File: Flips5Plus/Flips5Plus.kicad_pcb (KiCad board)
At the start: 2 copper layers, 80 x 75 mm, 8 parts, among them CN1 Conn_02x30_Odd_Even, CN2 UFP2810, CN3 UFP2810, U1 FP2800A, U2 FP2800A

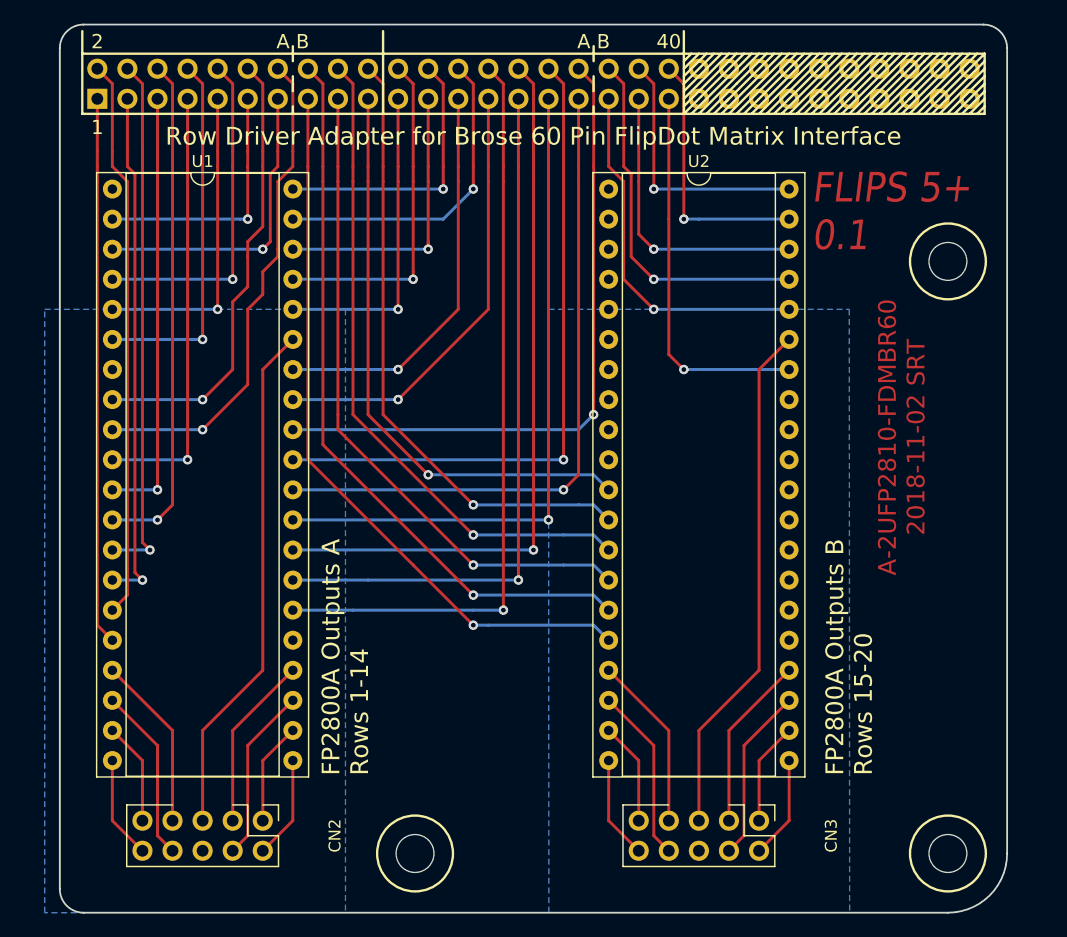
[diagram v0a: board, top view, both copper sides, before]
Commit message: using ANGLED shrouded header
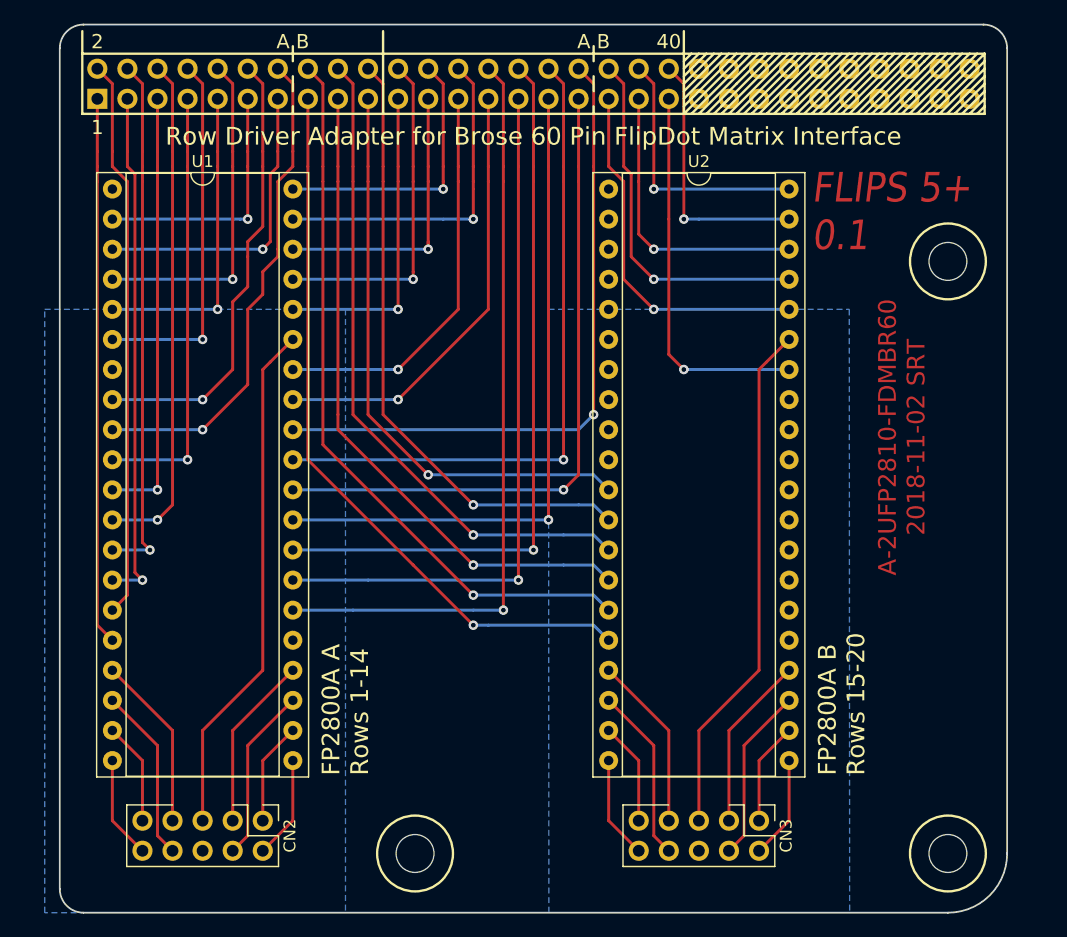
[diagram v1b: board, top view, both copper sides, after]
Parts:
- CN2, CN3: footprint Own:Pin_Header_Straight_Shrouded_2x05_Pitch2.54mm -> Own:Pin_Header_Angle_Shrouded_2x05_Pitch2.54mm
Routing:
- net Net-(CN1-Pad26): track 27.0 -> 28.5 mm
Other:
- board text added: "FP2800A A Rows 1-14"
- board text added: "FP2800A B Rows 15-20"
- board text removed: "FP2800A Outputs A Rows 1-14"
- board text removed: "FP2800A Outputs B Rows 15-20"

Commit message: adding logos and 3d models
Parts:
- added REF**: KiCAD Logo, Symbols:Symbol_KiCAD-Logo_CopperAndSilkScreenTop, F.Cu at (143.5, 115.6)
- added REF***: OSHW-Logo2_7.3x6mm_SilkScreen, Symbols:OSHW-Logo2_7.3x6mm_SilkScreen, F.Cu at (143.5, 130.2)
- added REF***: WEEE-Logo_4.2x6mm_SilkScreen, Symbols:WEEE-Logo_4.2x6mm_SilkScreen, B.Cu at (105.4, 147.3)
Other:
- board text added: "FLIPS"
- board text added: "FP2800A A: Rows 1-14"
- board text added: "FP2800A B: Rows 15-20"
- board text added: "SRT Flips 5Plus V1.0 2018-11-02 github.com/cawapy/FlipSuite"
- board text added: "back"
- board text added: "front"
- board text removed: "A-2UFP2810-FDMBR60 2018-11-02 SRT"
- board text removed: "FLIPS 5+ 0.1"
- board text removed: "FP2800A A Rows 1-14"
- board text removed: "FP2800A B Rows 15-20"

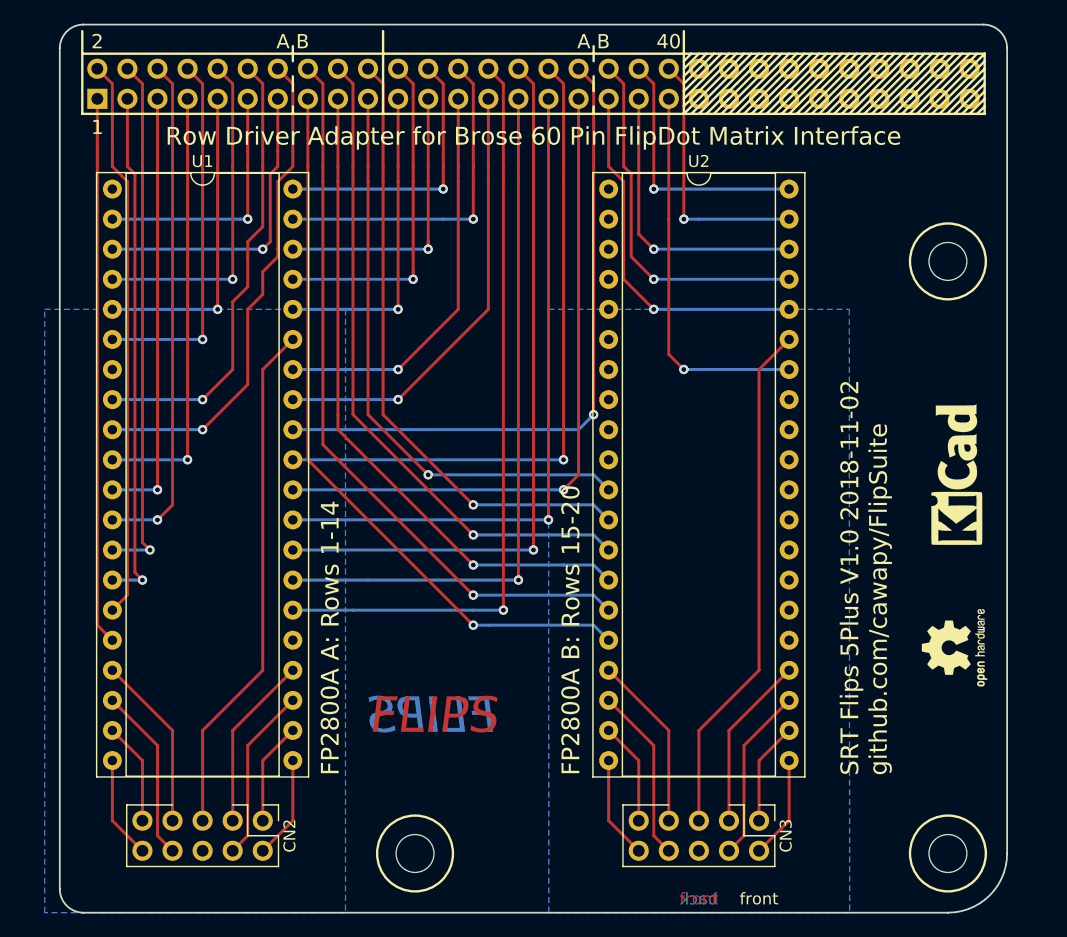
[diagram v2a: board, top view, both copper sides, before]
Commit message: rearranging mounting holes and symbols fixing measurements
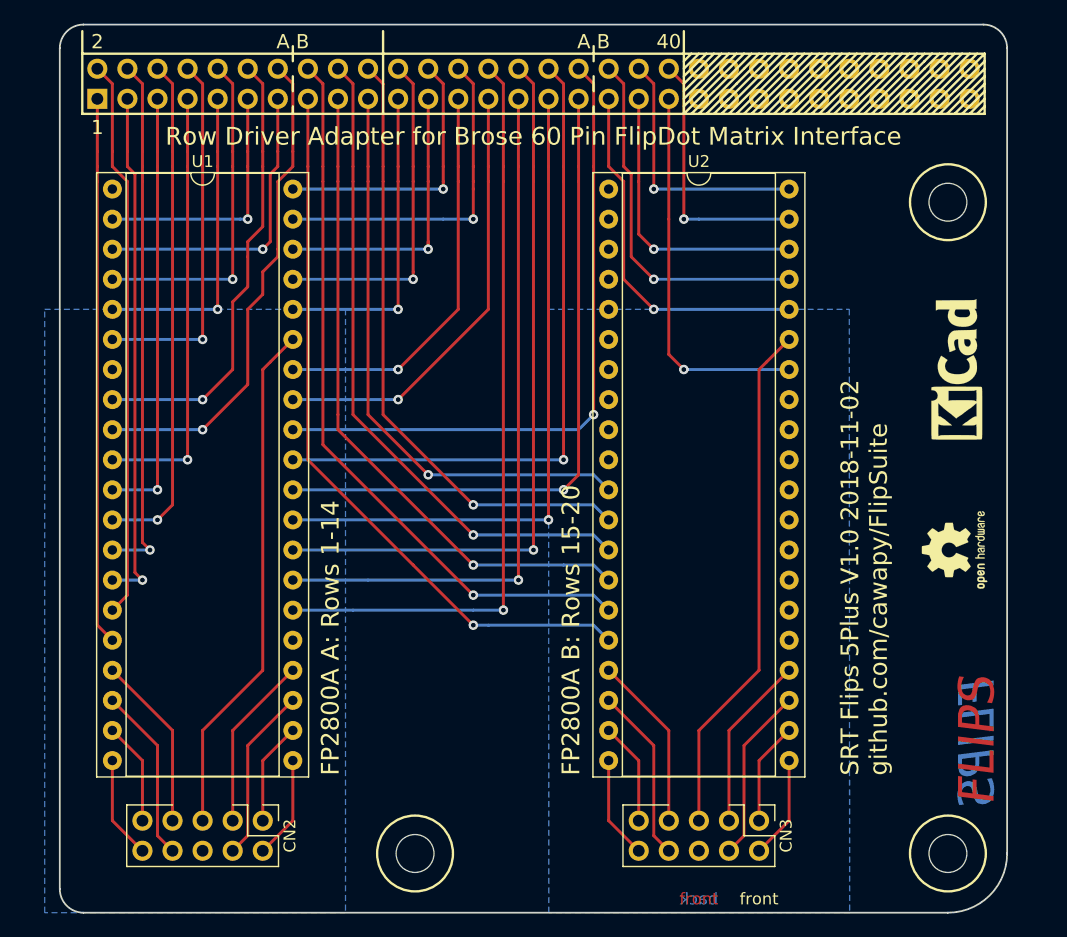
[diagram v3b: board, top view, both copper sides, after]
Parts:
- moved REF** 8.89 mm to (143.5, 106.7)
- moved REF*** 8.26 mm to (143.5, 121.9)
- moved REF** 5.00 mm to (142.9, 92.5)
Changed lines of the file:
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@@
   (general
     (thickness 1.6)
-    (drawings 117)
+    (drawings 116)
     (tracks 320)
     (zones 0)
@@
   )
   (module Mounting_Holes:MountingHole_3.2mm_M3 (layer F.Cu)
-    (at 142.95 97.55)
+    (at 142.95 92.55)
     (descr "Mounting Hole 3.2mm, no annular, M3")
     (tags "mounting hole 3.2mm no annular m3")
@@
   )
   (module Symbols:Symbol_KiCAD-Logo_CopperAndSilkScreenTop (layer F.Cu)
-    (at 143.51 115.57 90)
+    (at 143.51 106.68 90)
     (descr "Symbol, KiCAD-Logo, Silk & Copper Top,")
     (tags "Symbol, KiCAD-Logo, Silk & Copper Top,")
@@
   )
   (module Symbols:OSHW-Logo2_7.3x6mm_SilkScreen (layer F.Cu)
-    (at 143.51 130.175 90)
+    (at 143.51 121.92 90)
     (descr "Open Source Hardware Symbol")
     (tags "Logo Symbol OSHW")
@@
       (xy 1.530863 2.420002) (xy 1.583231 2.473048) (xy 2.125049 3.022233) (xy 2.12443 2.935152)) (layer B.SilkS) (width 0.01))
   )
+  (dimension 5 (width 0.3) (layer Dwgs.User)
+    (gr_text "5 mm" (at 164.05 150.05 270) (layer Dwgs.User)
+      (effects (font (size 1.5 1.5) (thickness 0.3)))
+    )
+    (feature1 (pts (xy 153.95 152.55) (xy 162.536421 152.55)))
+    (feature2 (pts (xy 153.95 147.55) (xy 162.536421 147.55)))
+    (crossbar (pts (xy 161.95 147.55) (xy 161.95 152.55)))
+    (arrow1a (pts (xy 161.95 152.55) (xy 161.363579 151.423496)))
+    (arrow1b (pts (xy 161.95 152.55) (xy 162.536421 151.423496)))
+    (arrow2a (pts (xy 161.95 147.55) (xy 161.363579 148.676504)))
+    (arrow2b (pts (xy 161.95 147.55) (xy 162.536421 148.676504)))
+  )
+  (dimension 55 (width 0.3) (layer Dwgs.User)
+    (gr_text "55 mm" (at 164.05 120.05 270) (layer Dwgs.User)
+      (effects (font (size 1.5 1.5) (thickness 0.3)))
+    )
+    (feature1 (pts (xy 153.95 147.55) (xy 162.536421 147.55)))
+    (feature2 (pts (xy 153.95 92.55) (xy 162.536421 92.55)))
+    (crossbar (pts (xy 161.95 92.55) (xy 161.95 147.55)))
+    (arrow1a (pts (xy 161.95 147.55) (xy 161.363579 146.423496)))
+    (arrow1b (pts (xy 161.95 147.55) (xy 162.536421 146.423496)))
+    (arrow2a (pts (xy 161.95 92.55) (xy 161.363579 93.676504)))
+    (arrow2b (pts (xy 161.95 92.55) (xy 162.536421 93.676504)))
+  )
+  (dimension 15 (width 0.3) (layer Dwgs.User)
+    (gr_text "15 mm" (at 164.05 85.05 270) (layer Dwgs.User)
+      (effects (font (size 1.5 1.5) (thickness 0.3)))
+    )
+    (feature1 (pts (xy 153.95 92.55) (xy 162.536421 92.55)))
+    (feature2 (pts (xy 153.95 77.55) (xy 162.536421 77.55)))
+    (crossbar (pts (xy 161.95 77.55) (xy 161.95 92.55)))
+    (arrow1a (pts (xy 161.95 92.55) (xy 161.363579 91.423496)))
+    (arrow1b (pts (xy 161.95 92.55) (xy 162.536421 91.423496)))
+    (arrow2a (pts (xy 161.95 77.55) (xy 161.363579 78.676504)))
+    (arrow2b (pts (xy 161.95 77.55) (xy 162.536421 78.676504)))
+  )
+  (dimension 75 (width 0.3) (layer Dwgs.User)
+    (gr_text "75 mm" (at 48.85 115.05 90) (layer Dwgs.User)
+      (effects (font (size 1.5 1.5) (thickness 0.3)))
+    )
+    (feature1 (pts (xy 58.95 77.55) (xy 50.363579 77.55)))
+    (feature2 (pts (xy 58.95 152.55) (xy 50.363579 152.55)))
+    (crossbar (pts (xy 50.95 152.55) (xy 50.95 77.55)))
+    (arrow1a (pts (xy 50.95 77.55) (xy 51.536421 78.676504)))
+    (arrow1b (pts (xy 50.95 77.55) (xy 50.363579 78.676504)))
+    (arrow2a (pts (xy 50.95 152.55) (xy 51.536421 151.423496)))
+    (arrow2b (pts (xy 50.95 152.55) (xy 50.363579 151.423496)))
+  )
   (gr_text back (at 127 151.384) (layer B.SilkS)
     (effects (font (size 1 1) (thickness 0.25)) (justify mirror))
@@
     (effects (font (size 1 1) (thickness 0.25)) (justify mirror))
   )
-  (gr_text FLIPS (at 93.98 135.89) (layer B.Cu)
+  (gr_text FLIPS (at 145.415 143.51 90) (layer B.Cu)
     (effects (font (size 3 3) (thickness 0.75) italic) (justify right mirror))
   )
-  (gr_text FLIPS (at 93.98 135.89) (layer F.Cu)
+  (gr_text FLIPS (at 145.415 143.51 90) (layer F.Cu)
     (effects (font (size 3 3) (thickness 0.75) italic) (justify left))
   )
@@
   (gr_circle (center 97.95 147.55) (end 100.45 145.55) (layer B.SilkS) (width 0.2))
   (gr_circle (center 142.95 147.55) (end 145.45 145.55) (layer B.SilkS) (width 0.2))
-  (gr_circle (center 142.95 97.55) (end 145.45 95.55) (layer B.SilkS) (width 0.2))
-  (gr_circle (center 142.95 97.55) (end 145.45 95.55) (layer F.SilkS) (width 0.2))
+  (gr_circle (center 142.95 92.55) (end 145.45 90.55) (layer B.SilkS) (width 0.2))
+  (gr_circle (center 142.95 92.55) (end 145.45 90.55) (layer F.SilkS) (width 0.2))
   (gr_circle (center 142.95 147.55) (end 145.45 145.55) (layer F.SilkS) (width 0.2))
   (gr_circle (center 97.95 147.55) (end 100.45 145.55) (layer F.SilkS) (width 0.2))
   (gr_text "SRT Flips 5Plus V1.0 2018-11-02\ngithub.com/cawapy/FlipSuite" (at 135.89 140.97 90) (layer F.SilkS)
     (effects (font (size 1.5 1.5) (thickness 0.3)) (justify left))
-  )
-  (dimension 55 (width 0.3) (layer Dwgs.User)
-    (gr_text "55 mm" (at 48.85 105.05 270) (layer Dwgs.User)
-      (effects (font (size 1.5 1.5) (thickness 0.3)))
-    )
-    (feature1 (pts (xy 58.95 132.55) (xy 50.363579 132.55)))
-    (feature2 (pts (xy 58.95 77.55) (xy 50.363579 77.55)))
-    (crossbar (pts (xy 50.95 77.55) (xy 50.95 132.55)))
-    (arrow1a (pts (xy 50.95 132.55) (xy 50.363579 131.423496)))
-    (arrow1b (pts (xy 50.95 132.55) (xy 51.536421 131.423496)))
-    (arrow2a (pts (xy 50.95 77.55) (xy 50.363579 78.676504)))
-    (arrow2b (pts (xy 50.95 77.55) (xy 51.536421 78.676504)))
-  )
-  (dimension 5 (width 0.3) (layer Dwgs.User)
-    (gr_text "5 mm" (at 171.05 130.05 270) (layer Dwgs.User)
-      (effects (font (size 1.5 1.5) (thickness 0.3)))
-    )
-    (feature1 (pts (xy 162.95 132.55) (xy 169.536421 132.55)))
-    (feature2 (pts (xy 162.95 127.55) (xy 169.536421 127.55)))
-    (crossbar (pts (xy 168.95 127.55) (xy 168.95 132.55)))
-    (arrow1a (pts (xy 168.95 132.55) (xy 168.363579 131.423496)))
-    (arrow1b (pts (xy 168.95 132.55) (xy 169.536421 131.423496)))
-    (arrow2a (pts (xy 168.95 127.55) (xy 168.363579 128.676504)))
-    (arrow2b (pts (xy 168.95 127.55) (xy 169.536421 128.676504)))
-  )
-  (dimension 30 (width 0.3) (layer Dwgs.User)
-    (gr_text "30 mm" (at 171.05 112.55 270) (layer Dwgs.User)
-      (effects (font (size 1.5 1.5) (thickness 0.3)))
-    )
-    (feature1 (pts (xy 162.95 127.55) (xy 169.536421 127.55)))
-    (feature2 (pts (xy 162.95 97.55) (xy 169.536421 97.55)))
-    (crossbar (pts (xy 168.95 97.55) (xy 168.95 127.55)))
-    (arrow1a (pts (xy 168.95 127.55) (xy 168.363579 126.423496)))
-    (arrow1b (pts (xy 168.95 127.55) (xy 169.536421 126.423496)))
-    (arrow2a (pts (xy 168.95 97.55) (xy 168.363579 98.676504)))
-    (arrow2b (pts (xy 168.95 97.55) (xy 169.536421 98.676504)))
-  )
-  (dimension 15 (width 0.3) (layer Dwgs.User)
-    (gr_text "15 mm" (at 171.05 90.05 270) (layer Dwgs.User)
-      (effects (font (size 1.5 1.5) (thickness 0.3)))
-    )
-    (feature1 (pts (xy 162.95 97.55) (xy 169.536421 97.55)))
-    (feature2 (pts (xy 162.95 82.55) (xy 169.536421 82.55)))
-    (crossbar (pts (xy 168.95 82.55) (xy 168.95 97.55)))
-    (arrow1a (pts (xy 168.95 97.55) (xy 168.363579 96.423496)))
-    (arrow1b (pts (xy 168.95 97.55) (xy 169.536421 96.423496)))
-    (arrow2a (pts (xy 168.95 82.55) (xy 168.363579 83.676504)))
-    (arrow2b (pts (xy 168.95 82.55) (xy 169.536421 83.676504)))
   )
   (gr_line (start 147.95 79.55) (end 147.95 147.55) (layer Edge.Cuts) (width 0.15))
@@
     (arrow2b (pts (xy 142.95 159.55) (xy 144.076504 158.963579)))
   )
-  (dimension 5 (width 0.3) (layer Dwgs.User)
-    (gr_text "5 mm" (at 171.05 80.05 270) (layer Dwgs.User)
-      (effects (font (size 1.5 1.5) (thickness 0.3)))
-    )
-    (feature1 (pts (xy 162.95 82.55) (xy 169.536421 82.55)))
-    (feature2 (pts (xy 162.95 77.55) (xy 169.536421 77.55)))
-    (crossbar (pts (xy 168.95 77.55) (xy 168.95 82.55)))
-    (arrow1a (pts (xy 168.95 82.55) (xy 168.363579 81.423496)))
-    (arrow1b (pts (xy 168.95 82.55) (xy 169.536421 81.423496)))
-    (arrow2a (pts (xy 168.95 77.55) (xy 168.363579 78.676504)))
-    (arrow2b (pts (xy 168.95 77.55) (xy 169.536421 78.676504)))
-  )
   (gr_arc (start 142.95 147.55) (end 147.95 147.55) (angle 90) (layer Edge.Cuts) (width 0.15))
